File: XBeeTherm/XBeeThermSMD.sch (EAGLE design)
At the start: 18 parts

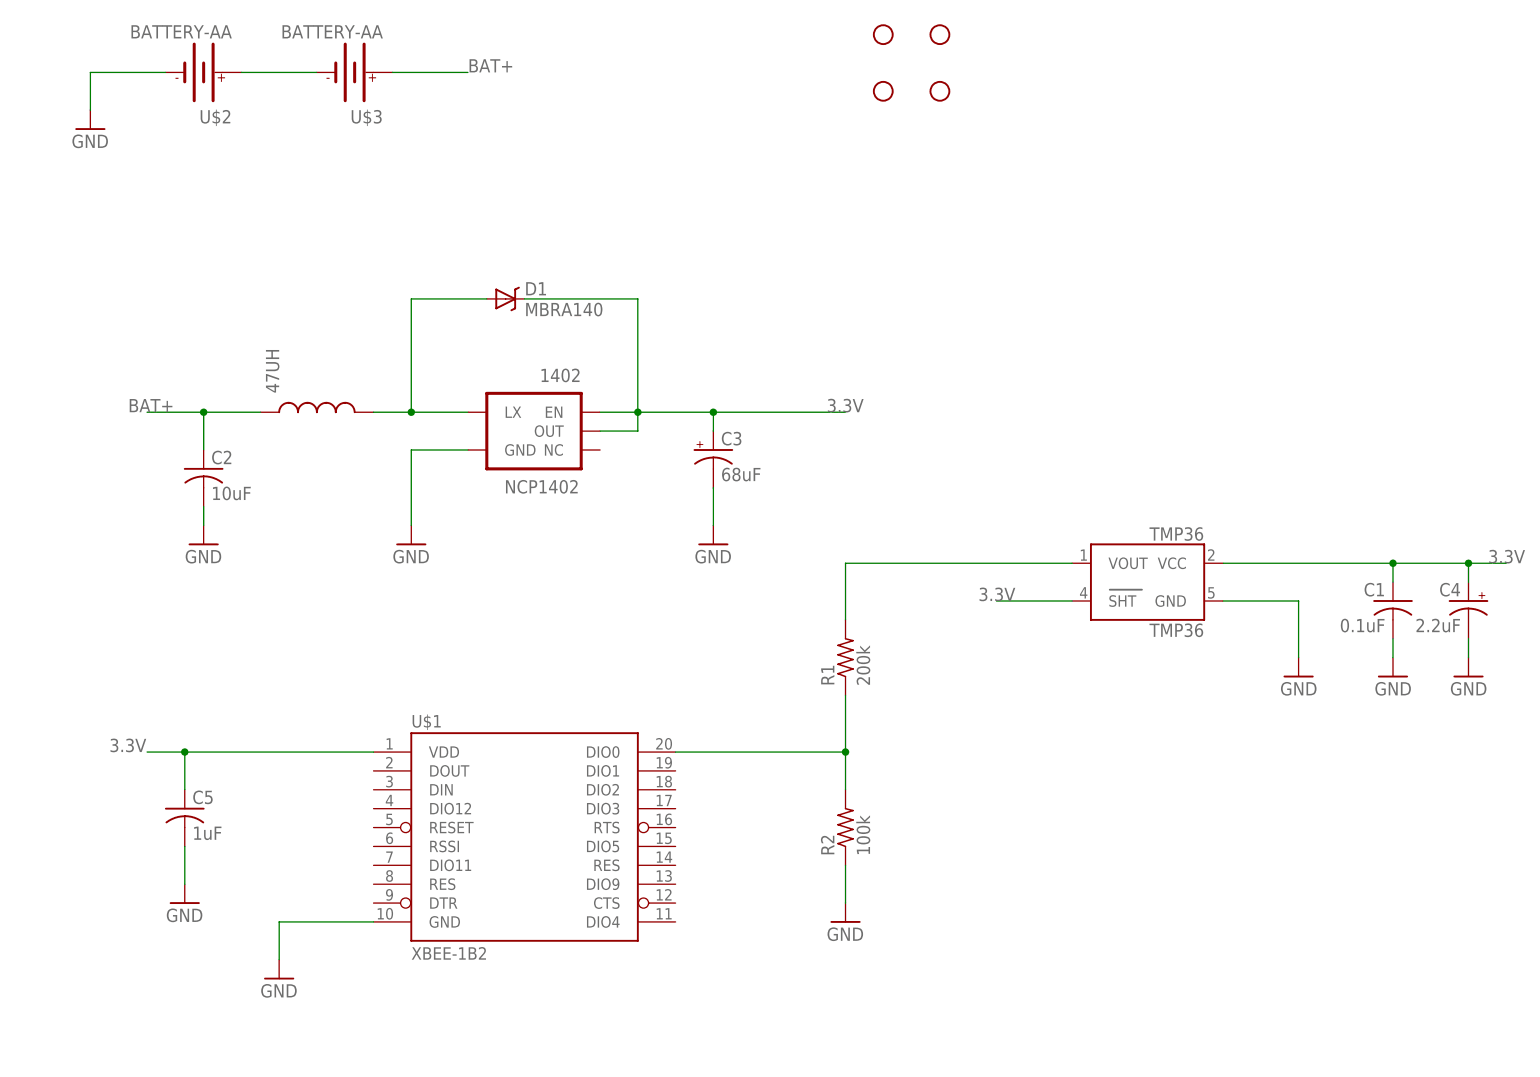
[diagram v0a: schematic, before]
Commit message: First fab of the XBee therm board
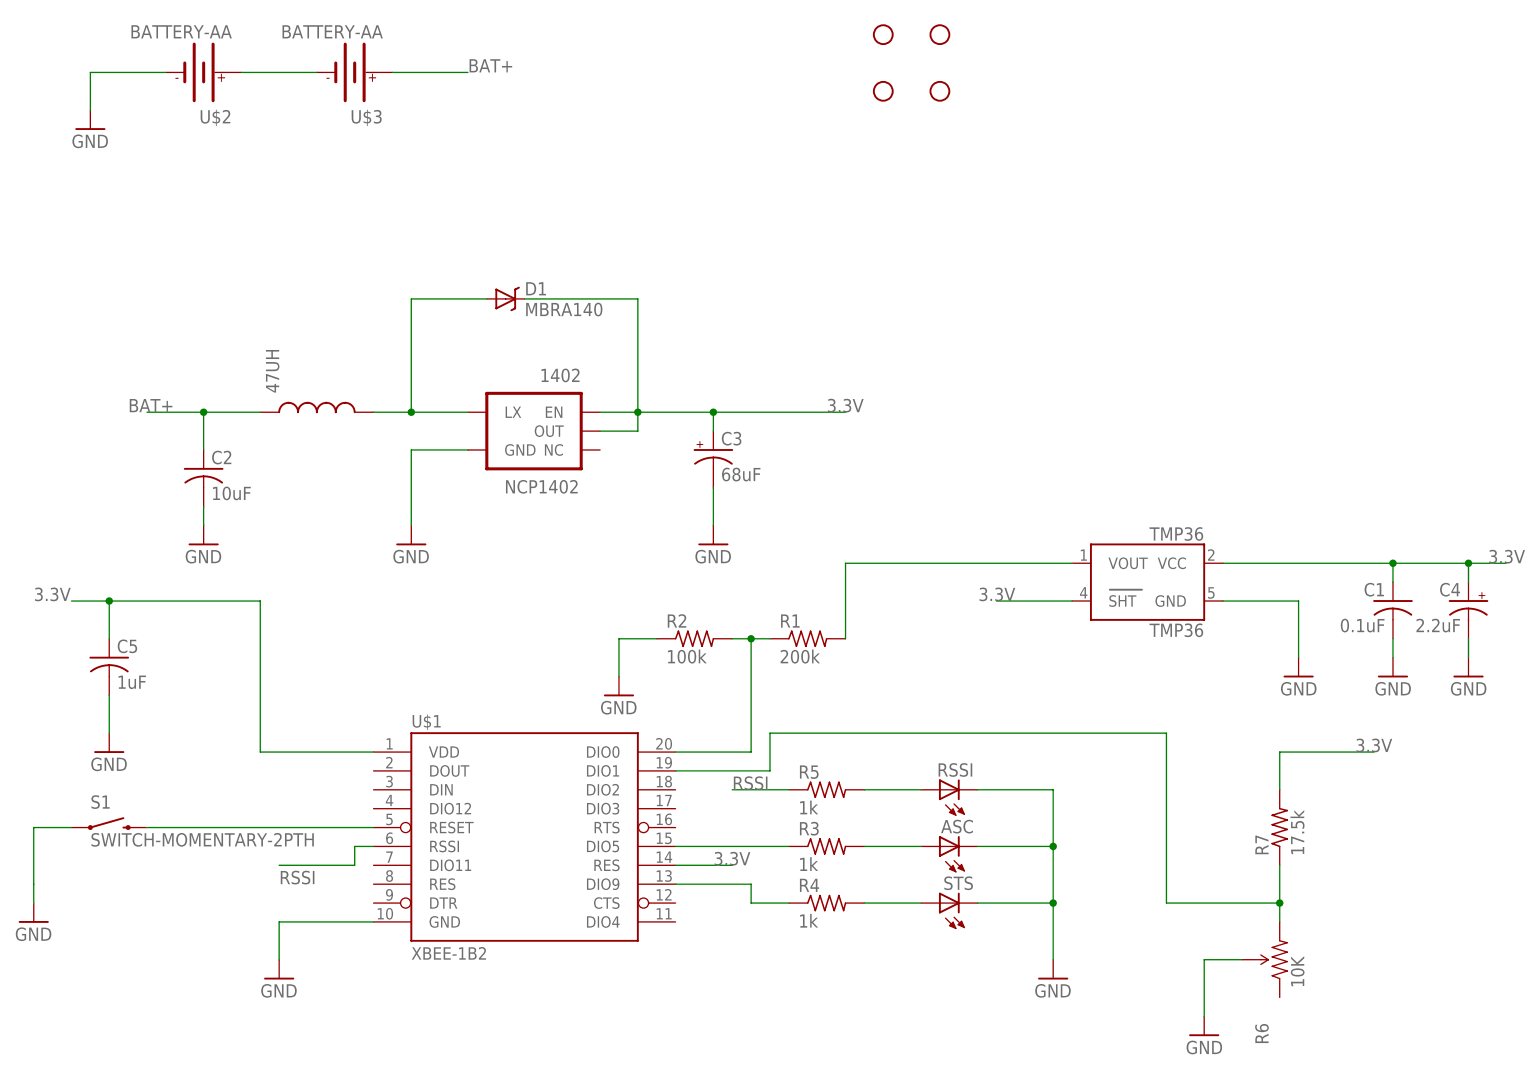
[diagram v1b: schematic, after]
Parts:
- added ASC, RSSI, STS: (no value), led:LEDCHIP-LED0603
- added R3, R4, R5: 1k, resistor:R-US_R0603
- added R6: 10K, SparkFun-Electromechanical:TRIMPOT-2
- added R7: 17.5k, resistor:R-US_R0603
- added S1: SWITCH-MOMENTARY-2PTH, SparkFun-Electromechanical:SWITCH-MOMENTARY-2PTH
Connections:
- new net N$10: S1.2, U$1.RESET
- new net N$13: R5.2, RSSI.A
- new net N$5: R3.1, U$1.DIO5
- new net N$6: R4.1, U$1.DIO9
- new net N$7: ASC.A, R3.2
- new net N$8: R4.2, STS.A
- new net N$9: R6.CW, R7.1, U$1.DIO1
- new net RSSI: R5.1, U$1.RSSI
- net 3.3V: now also R7.2, U$1.RES@14
- net GND: now also ASC.C, R6.WIPER, RSSI.C, S1.1, STS.C
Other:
- moved on the sheet: C5, R1, R2

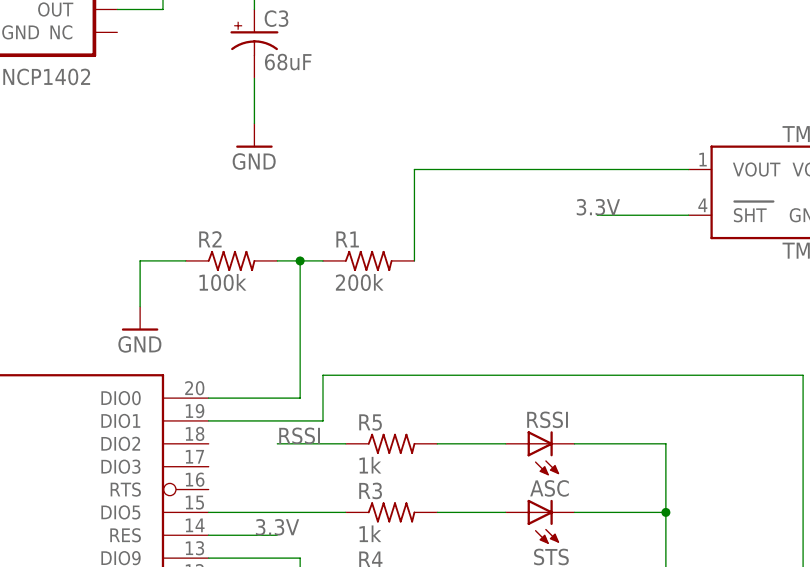
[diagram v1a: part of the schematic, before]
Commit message: Update for the 0 ohm jumper change to the board
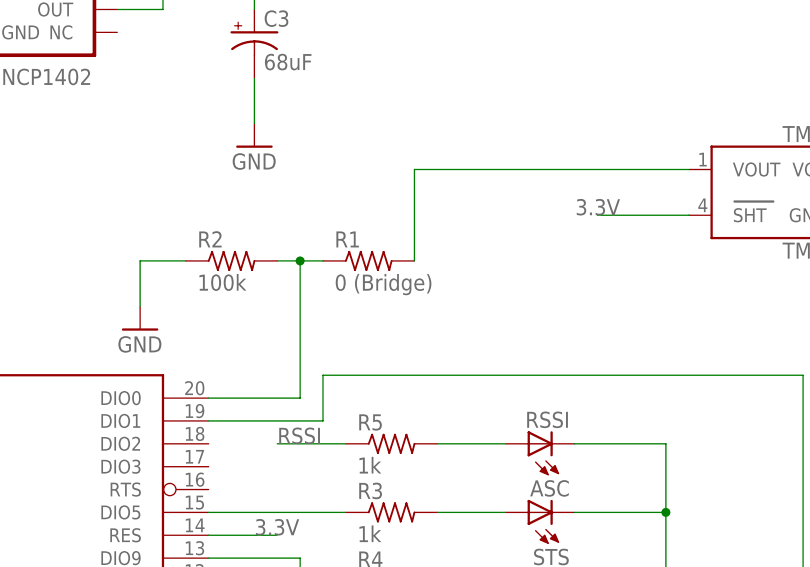
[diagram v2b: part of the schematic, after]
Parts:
- R1: value 200k -> 0 (Bridge)
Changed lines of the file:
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@@
 <part name="C4" library="resistor" deviceset="CPOL-US" device="R/2012-12R" value="2.2uF"/>
 <part name="GND8" library="SparkFun-Aesthetics" deviceset="GND" device=""/>
-<part name="R1" library="resistor" deviceset="R-US_" device="R0603" value="200k"/>
+<part name="R1" library="resistor" deviceset="R-US_" device="R0603" value="0 (Bridge)"/>
 <part name="R2" library="resistor" deviceset="R-US_" device="R0603" value="100k"/>
 <part name="GND9" library="SparkFun-Aesthetics" deviceset="GND" device=""/>
